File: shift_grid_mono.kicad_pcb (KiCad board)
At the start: 2 copper layers, 53.3 x 68.6 mm, 152 parts, among them J1 Conn_01x08, U1 74HC595, U2 74HC595

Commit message: Fix messed up rows 3,4
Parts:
- moved D83 3.81 mm to (92.7, 86.4)
- moved D84 3.81 mm to (87.6, 86.4)
- moved D87 3.81 mm to (92.7, 82.5)
- moved D88 3.81 mm to (87.6, 82.5)
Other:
- board text added: "v0.0.1 04/30/20"
- board text removed: "v0.0.0 04/30/20"
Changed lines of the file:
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@@
   )
   (setup
-    (last_trace_width 0.3)
+    (last_trace_width 0.25)
     (user_trace_width 0.3)
     (trace_clearance 0.2)
@@
   )
   (module LED_SMD:LED_0805_2012Metric (layer F.Cu)
-    (at 87.63 86.36 180)
+    (at 87.63 82.55 180)
     (descr "LED SMD 0805 (2012 Metric), square (rectangular) end terminal, IPC_7351 nominal, (Body size source: https://docs.google.com/spreadsheets/d/1BsfQQcO9C6DZCsRaXUlFlo91Tg2WpOkGARC1WS5S8t0/edit?usp=sharing), generated with kicad-footprint-generator")
     (tags diode)
@@
   )
   (module LED_SMD:LED_0805_2012Metric (layer F.Cu)
-    (at 92.71 86.36 180)
+    (at 92.71 82.55 180)
     (descr "LED SMD 0805 (2012 Metric), square (rectangular) end terminal, IPC_7351 nominal, (Body size source: https://docs.google.com/spreadsheets/d/1BsfQQcO9C6DZCsRaXUlFlo91Tg2WpOkGARC1WS5S8t0/edit?usp=sharing), generated with kicad-footprint-generator")
     (tags diode)
@@
   )
   (module LED_SMD:LED_0805_2012Metric (layer F.Cu)
-    (at 87.63 82.55)
+    (at 87.63 86.36)
     (descr "LED SMD 0805 (2012 Metric), square (rectangular) end terminal, IPC_7351 nominal, (Body size source: https://docs.google.com/spreadsheets/d/1BsfQQcO9C6DZCsRaXUlFlo91Tg2WpOkGARC1WS5S8t0/edit?usp=sharing), generated with kicad-footprint-generator")
     (tags diode)
@@
   )
   (module LED_SMD:LED_0805_2012Metric (layer F.Cu)
-    (at 92.71 82.55)
+    (at 92.71 86.36)
     (descr "LED SMD 0805 (2012 Metric), square (rectangular) end terminal, IPC_7351 nominal, (Body size source: https://docs.google.com/spreadsheets/d/1BsfQQcO9C6DZCsRaXUlFlo91Tg2WpOkGARC1WS5S8t0/edit?usp=sharing), generated with kicad-footprint-generator")
     (tags diode)
@@
     (effects (font (size 1 1) (thickness 0.2)) (justify left))
   )
-  (gr_text "      v0.0.0\n04/30/20" (at 78.105 120.015 90) (layer F.SilkS)
+  (gr_text "      v0.0.1\n04/30/20" (at 78.105 120.015 90) (layer F.SilkS)
     (effects (font (size 1.5 1.5) (thickness 0.3)))
   )

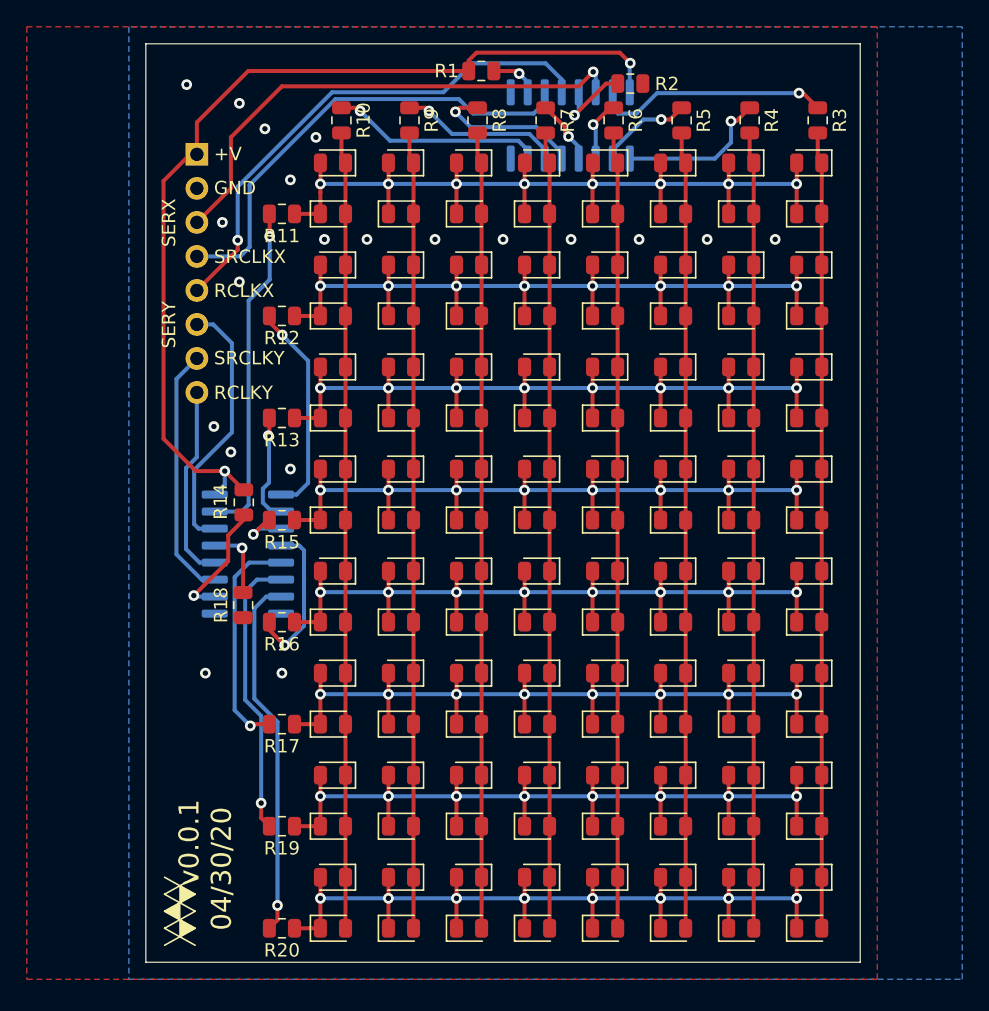
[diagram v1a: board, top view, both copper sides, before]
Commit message: Reduce LEDs by half
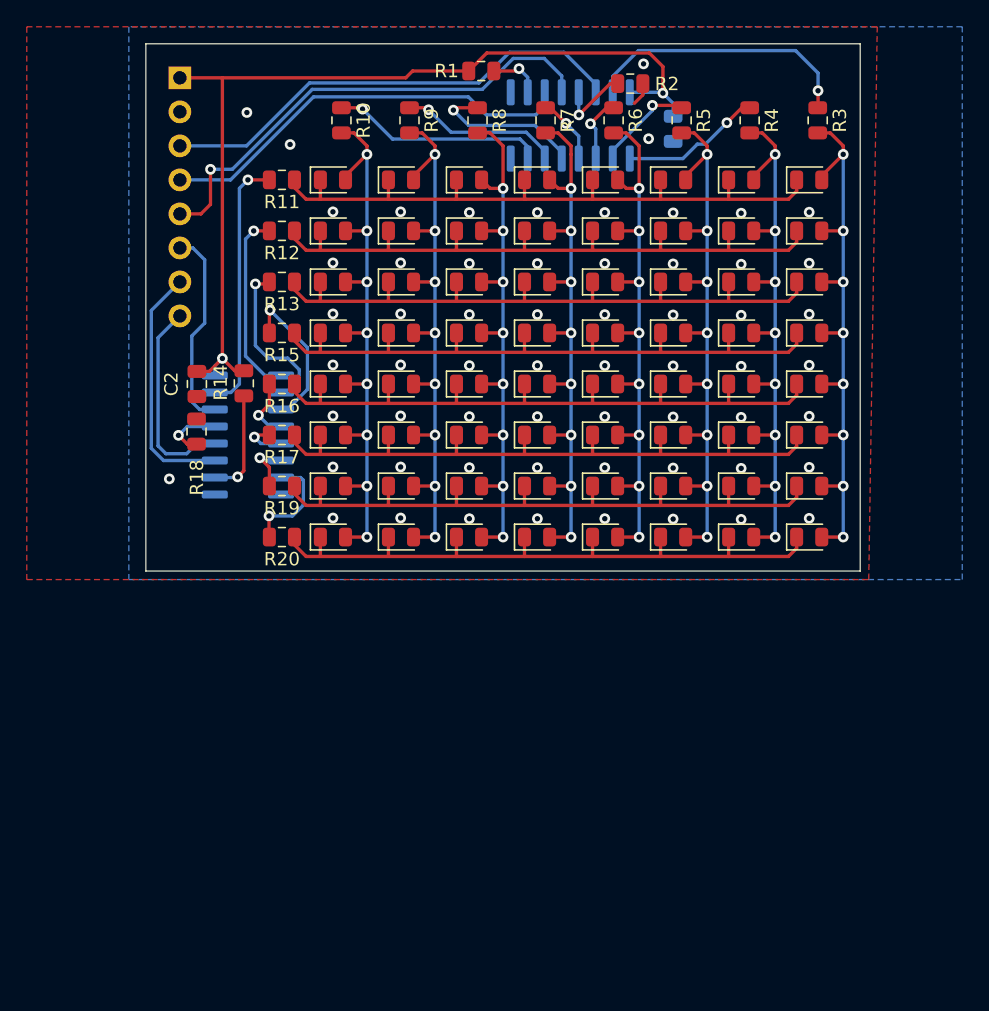
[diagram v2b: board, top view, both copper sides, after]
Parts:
- removed D101, D102, D103, D104, D109, D110, D111, D112, D117, D118, D119, D120, D125, D126, D127, D128, D13, D14, D15, D16, D21, D22, D23, D24, D29, D30, D31, D32, D37, D38, D39, D40, D45, D46, D47, D48, D5, D53, D54, D55, D56, D6, D61, D62, D63, D64, D69, D7, D70, D71, D72, D77, D78, D79, D8, D80, D85, D86, D87, D88, D93, D94, D95, D96: LED, LED_SMD:LED_0805_2012Metric
- added C1: 10kpF, Capacitor_SMD:C_0805_2012Metric, B.Cu at (113.0, 64.8)
- added C2: 10kpF, Capacitor_SMD:C_0805_2012Metric, F.Cu at (77.5, 83.8)
- REF**: moved to B.Cu
- moved REF** 61.7 mm to (85.7, 62.2), turned to 0 degrees
- moved D121 29.2 mm to (102.9, 95.2)
- moved D122 29.2 mm to (97.8, 95.2)
- moved D123 29.2 mm to (92.7, 95.2)
- moved D124 29.2 mm to (87.6, 95.2)
- moved D57 29.2 mm to (123.2, 95.2)
- moved D58 29.2 mm to (118.1, 95.2)
- moved D59 29.2 mm to (113.0, 95.2)
- moved D60 29.2 mm to (108.0, 95.2)
- moved R20 29.2 mm to (83.8, 95.2)
- moved D113 25.4 mm to (102.9, 91.4)
- moved D114 25.4 mm to (97.8, 91.4)
- moved D115 25.4 mm to (92.7, 91.4)
- moved D116 25.4 mm to (87.6, 91.4)
- moved D49 25.4 mm to (123.2, 91.4)
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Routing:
- net Net-(R20-Pad2): track 27.2 -> 8.09 mm
- net /4x4_0-0/Y3: track 68.0 -> 49.7 mm, vias 8 -> 0
- net /4x4_0-0/Y2: track 68.0 -> 49.7 mm, vias 8 -> 0
- net /4x4_0-1/Y2: track 68.0 -> 49.7 mm, vias 8 -> 0
- net /4x4_0-0/Y0: track 68.0 -> 49.7 mm, vias 8 -> 0
- net /4x4_0-1/Y1: track 68.0 -> 49.7 mm, vias 8 -> 0
- net /4x4_0-1/Y3: track 68.0 -> 49.7 mm, vias 8 -> 0
- net /4x4_0-0/Y1: track 68.0 -> 49.7 mm, vias 8 -> 0
- net /4x4_0-1/Y0: track 68.0 -> 49.7 mm, vias 8 -> 0
- net Net-(R19-Pad2): track 21.3 -> 4.07 mm
- net /4x4_1-0/X0: track 59.5 -> 44.6 mm, vias 0 -> 8
- net /4x4_0-0/X3: track 59.5 -> 44.6 mm, vias 0 -> 8
- net /4x4_1-0/X1: track 59.5 -> 44.9 mm, vias 0 -> 8
- net /4x4_0-0/X2: track 59.5 -> 45.3 mm, vias 0 -> 8
- net /4x4_1-0/X3: track 59.5 -> 45.3 mm, vias 0 -> 8
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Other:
- board size 53.3 x 68.6 mm -> 53.3 x 39.4 mm
- board text added: "v0.1.0 04/30/20"
- board text removed: "v0.0.1 04/30/20"

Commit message: Correct modify time
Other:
- board text added: "v0.1.0 05/14/20"
- board text removed: "v0.1.0 04/30/20"
